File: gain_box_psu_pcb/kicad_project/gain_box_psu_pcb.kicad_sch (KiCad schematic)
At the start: 78 parts, among them J1 Conn_01x02, J2 Conn_01x04, J3 Conn_01x03, J4 Conn_01x02, J5 Conn_01x02, J6 AVR-UPDI-6, K1 J107F1CS2012VDC.80, K2 J104D2C12VDC.36S, Q1 AO3400A, Q2 AO3400A, Q3 AO3400A, T1 70042K, U1 LM7809, U2 LM7909, U3 78L05, U4 140817141310, U5 ATtiny412-SS

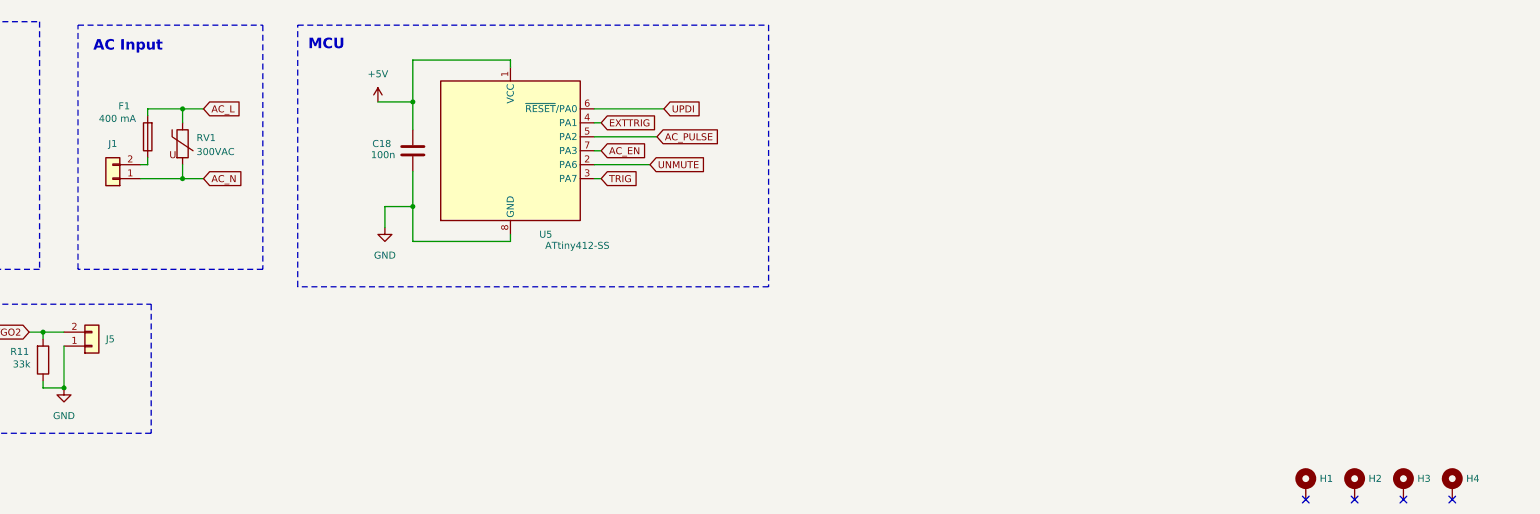
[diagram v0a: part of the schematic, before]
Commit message: Shorten PSU PCB
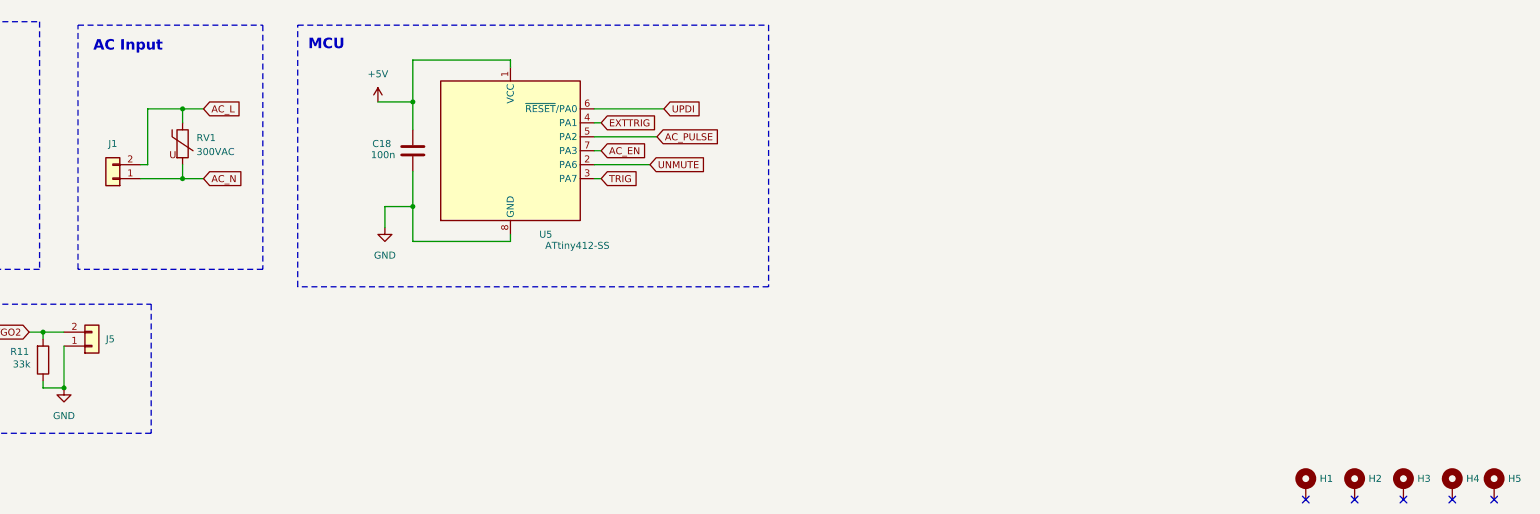
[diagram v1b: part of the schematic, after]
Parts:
- removed F1: 400 mA, Fuse:Fuseholder_Clip-5x20mm_Bel_FC-203-22_Lateral_P17.80x5.00mm_D1.17mm_Horizontal, symbol Device:Fuse
- added H5: MountingHole_Pad, MountingHole:MountingHole_3.2mm_M3_Pad_Via, symbol Mechanical:MountingHole_Pad
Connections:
- net AC_L: now also J1.2 (Pin_2)
- no-connect marks 6 -> 7
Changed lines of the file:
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@@
 	)
 	(no_connect
+		(at 397.51 246.38)
+	)
+	(no_connect
 		(at 363.22 246.38)
 	)
@@
 	(wire
 		(pts
-			(xy 152.4 175.26) (xy 152.4 176.53)
+			(xy 152.4 175.26) (xy 152.4 185.42)
 		)
 		(stroke
@@
 	(wire
 		(pts
-			(xy 152.4 184.15) (xy 152.4 185.42)
-		)
-		(stroke
-			(width 0)
-			(type default)
-		)
-	)
-	(wire
-		(pts
 			(xy 154.94 127) (xy 154.94 123.19)
 		)
@@
 	)
 	(symbol
+		(lib_id "Mechanical:MountingHole_Pad")
+		(at 397.51 243.84 0)
+		(unit 1)
+		(exclude_from_sim yes)
+		(in_bom no)
+		(on_board yes)
+		(dnp no)
+		(fields_autoplaced yes)
+		(property "Reference" "H5"
+			(at 400.05 242.5699 0)
+			(effects
+				(font
+					(size 1.27 1.27)
+				)
+				(justify left)
+			)
+		)
+		(property "Value" "MountingHole_Pad"
+			(at 400.05 243.8399 0)
+			(effects
+				(font
+					(size 1.27 1.27)
+				)
+				(justify left)
+				(hide yes)
+			)
+		)
+		(property "Footprint" "MountingHole:MountingHole_3.2mm_M3_Pad_Via"
+			(at 397.51 243.84 0)
+			(effects
+				(font
+					(size 1.27 1.27)
+				)
+				(hide yes)
+			)
+		)
+		(property "Datasheet" "~"
+			(at 397.51 243.84 0)
+			(effects
+				(font
+					(size 1.27 1.27)
+				)
+				(hide yes)
+			)
+		)
+		(property "Description" "Mounting Hole with connection"
+			(at 397.51 243.84 0)
+			(effects
+				(font
+					(size 1.27 1.27)
+				)
+				(hide yes)
+			)
+		)
+		(pin "1"
+		)
+		(instances
+			(project "gain_box_psu_pcb"
+				(path "/9bac93c0-f586-4b1c-8172-4868afdb9131"
+					(reference "H5")
+					(unit 1)
+				)
+			)
+		)
+	)
+	(symbol
 		(lib_id "Device:R")
 		(at 38.1 220.98 270)
@@
 					(unit 1)
 				)
-			)
-		)
-	)
-	(symbol
-		(lib_id "Device:Fuse")
-		(at 152.4 180.34 180)
-		(unit 1)
-		(exclude_from_sim no)
-		(in_bom yes)
-		(on_board yes)
-		(dnp no)
-		(property "Reference" "F1"
-			(at 147.066 174.752 0)
-			(effects
-				(font
-					(size 1.27 1.27)
-				)
-				(justify right)
-			)
-		)
-		(property "Value" "400 mA"
-			(at 143.51 177.038 0)
-			(effects
-				(font
-					(size 1.27 1.27)
-				)
-				(justify right)
-			)
-		)
-		(property "Footprint" "Fuse:Fuseholder_Clip-5x20mm_Bel_FC-203-22_Lateral_P17.80x5.00mm_D1.17mm_Horizontal"
-			(at 154.178 180.34 90)
-			(effects
-				(font
-					(size 1.27 1.27)
-				)
-				(hide yes)
-			)
-		)
-		(property "Datasheet" "~"
-			(at 152.4 180.34 0)
-			(effects
-				(font
-					(size 1.27 1.27)
-				)
-				(hide yes)
-			)
-		)
-		(property "Description" "Fuse"
-			(at 152.4 180.34 0)
-			(effects
-				(font
-					(size 1.27 1.27)
-				)
-				(hide yes)
-			)
-		)
-		(pin "2"
-		)
-		(pin "1"
-		)
-		(instances
-			(project ""
-				(path "/9bac93c0-f586-4b1c-8172-4868afdb9131"
-					(reference "F1")
-					(unit 1)
-				)

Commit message: Update PSU PCB
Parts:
- added H6: Screw_Terminal_01x01, project_lib:KEYSTONE_7760, symbol Connector:Screw_Terminal_01x01
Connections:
- net Earth: now reaches H2.1
- net Earth: now also H3.1, H6.1 (Pin_1)
- no-connect marks 7 -> 5
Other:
- moved on the sheet: H1, H2, H3
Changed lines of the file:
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@@
 	)
 	(junction
+		(at 358.14 236.22)
+		(diameter 0)
+		(color 0 0 0 0)
+	)
+	(junction
 		(at 69.85 69.85)
 		(diameter 0)
@@
 	)
 	(no_connect
-		(at 372.11 246.38)
-	)
-	(no_connect
 		(at 266.7 45.72)
 	)
@@
 	)
 	(no_connect
-		(at 363.22 246.38)
-	)
-	(no_connect
 		(at 381 246.38)
 	)
@@
 	(wire
 		(pts
+			(xy 349.25 236.22) (xy 358.14 236.22)
+		)
+		(stroke
+			(width 0)
+			(type default)
+		)
+	)
+	(wire
+		(pts
 			(xy 143.51 87.63) (xy 138.43 87.63)
 		)
@@
 	(wire
 		(pts
+			(xy 358.14 236.22) (xy 367.03 236.22)
+		)
+		(stroke
+			(width 0)
+			(type default)
+		)
+	)
+	(wire
+		(pts
 			(xy 73.66 137.16) (xy 73.66 139.7)
 		)
@@
 	(wire
 		(pts
+			(xy 358.14 236.22) (xy 358.14 241.3)
+		)
+		(stroke
+			(width 0)
+			(type default)
+		)
+	)
+	(wire
+		(pts
 			(xy 367.03 77.47) (xy 369.57 77.47)
 		)
@@
 	(wire
 		(pts
+			(xy 367.03 236.22) (xy 367.03 234.95)
+		)
+		(stroke
+			(width 0)
+			(type default)
+		)
+	)
+	(wire
+		(pts
 			(xy 378.46 113.03) (xy 378.46 115.57)
 		)
@@
 	(wire
 		(pts
+			(xy 349.25 234.95) (xy 349.25 236.22)
+		)
+		(stroke
+			(width 0)
+			(type default)
+		)
+	)
+	(wire
+		(pts
 			(xy 186.69 54.61) (xy 186.69 59.69)
 		)
@@
 		)
 	)
+	(wire
+		(pts
+			(xy 358.14 236.22) (xy 358.14 234.95)
+		)
+		(stroke
+			(width 0)
+			(type default)
+		)
+	)
 	(rectangle
 		(start 17.78 104.14)
@@
 	)
 	(symbol
+		(lib_id "power:Earth")
+		(at 358.14 241.3 0)
+		(unit 1)
+		(exclude_from_sim no)
+		(in_bom yes)
+		(on_board yes)
+		(dnp no)
+		(fields_autoplaced yes)
+		(property "Reference" "#PWR01"
+			(at 358.14 247.65 0)
+			(effects
+				(font
+					(size 1.27 1.27)
+				)
+				(hide yes)
+			)
+		)
+		(property "Value" "Earth"
+			(at 358.14 246.38 0)
+			(effects
+				(font
+					(size 1.27 1.27)
+				)
+			)
+		)
+		(property "Footprint" ""
+			(at 358.14 241.3 0)
+			(effects
+				(font
+					(size 1.27 1.27)
+				)
+				(hide yes)
+			)
+		)
+		(property "Datasheet" "~"
+			(at 358.14 241.3 0)
+			(effects
+				(font
+					(size 1.27 1.27)
+				)
+				(hide yes)
+			)
+		)
+		(property "Description" "Power symbol creates a global label with name \"Earth\""
+			(at 358.14 241.3 0)
+			(effects
+				(font
+					(size 1.27 1.27)
+				)
+				(hide yes)
+			)
+		)
+		(pin "1"
+		)
+		(instances
+			(project ""
+				(path "/9bac93c0-f586-4b1c-8172-4868afdb9131"
+					(reference "#PWR01")
+					(unit 1)
+				)
+			)
+		)
+	)
+	(symbol
 		(lib_id "power:+15V")
 		(at 194.31 39.37 0)
@@
 	(symbol
 		(lib_id "Mechanical:MountingHole_Pad")
-		(at 372.11 243.84 0)
+		(at 358.14 232.41 0)
 		(unit 1)
 		(exclude_from_sim yes)
@@
 		(fields_autoplaced yes)
 		(property "Reference" "H2"
-			(at 374.65 242.5699 0)
+			(at 360.68 231.1399 0)
 			(effects
 				(font
@@
 		)
 		(property "Value" "MountingHole_Pad"
-			(at 374.65 243.8399 0)
+			(at 360.68 232.4099 0)
 			(effects
 				(font
@@
 		)
 		(property "Footprint" "MountingHole:MountingHole_3.2mm_M3_Pad_Via"
-			(at 372.11 243.84 0)
+			(at 358.14 232.41 0)
 			(effects
 				(font
@@
 		)
 		(property "Datasheet" "~"
-			(at 372.11 243.84 0)
+			(at 358.14 232.41 0)
 			(effects
 				(font
@@
 		)
 		(property "Description" "Mounting Hole with connection"
-			(at 372.11 243.84 0)
+			(at 358.14 232.41 0)
 			(effects
 				(font
@@
 	(symbol
 		(lib_id "Mechanical:MountingHole_Pad")
-		(at 381 243.84 0)
+		(at 367.03 232.41 0)
 		(unit 1)
 		(exclude_from_sim yes)
@@
 		(fields_autoplaced yes)
 		(property "Reference" "H3"
-			(at 383.54 242.5699 0)
+			(at 369.57 231.1399 0)
 			(effects
 				(font
@@
 		)
 		(property "Value" "MountingHole_Pad"
-			(at 383.54 243.8399 0)
+			(at 369.57 232.4099 0)
 			(effects
 				(font
@@
 		)
 		(property "Footprint" "MountingHole:MountingHole_3.2mm_M3_Pad_Via"
-			(at 381 243.84 0)
+			(at 367.03 232.41 0)
 			(effects
 				(font
@@
 		)
 		(property "Datasheet" "~"
-			(at 381 243.84 0)
+			(at 367.03 232.41 0)
 			(effects
 				(font
@@
 		)
 		(property "Description" "Mounting Hole with connection"
-			(at 381 243.84 0)
+			(at 367.03 232.41 0)
 			(effects
 				(font
@@
 	(symbol
 		(lib_id "Mechanical:MountingHole_Pad")
-		(at 363.22 243.84 0)
+		(at 381 243.84 0)
 		(unit 1)
 		(exclude_from_sim yes)
@@
 		(fields_autoplaced yes)
 		(property "Reference" "H1"
-			(at 365.76 242.5699 0)
+			(at 383.54 242.5699 0)
 			(effects
 				(font
@@
 		)
 		(property "Value" "MountingHole_Pad"
-			(at 365.76 243.8399 0)
+			(at 383.54 243.8399 0)
 			(effects
 				(font
@@
 		)
 		(property "Footprint" "MountingHole:MountingHole_3.2mm_M3_Pad_Via"
-			(at 363.22 243.84 0)
+			(at 381 243.84 0)
 			(effects
 				(font
@@
 		)
 		(property "Datasheet" "~"
-			(at 363.22 243.84 0)
+			(at 381 243.84 0)
 			(effects
 				(font
@@
 		)
 		(property "Description" "Mounting Hole with connection"
-			(at 363.22 243.84 0)
+			(at 381 243.84 0)
 			(effects
 				(font
@@
 					(unit 1)
 				)
+			)
+		)
+	)
+	(symbol
+		(lib_id "Connector:Screw_Terminal_01x01")
+		(at 349.25 229.87 90)
+		(unit 1)
+		(exclude_from_sim no)
+		(in_bom yes)
+		(on_board yes)
+		(dnp no)
+		(fields_autoplaced yes)
+		(property "Reference" "H6"
+			(at 351.79 229.8699 90)
+			(effects
+				(font
+					(size 1.27 1.27)
+				)
+				(justify right)
+			)
+		)
+		(property "Value" "Screw_Terminal_01x01"
+			(at 350.5199 227.33 0)
+			(effects
+				(font
+					(size 1.27 1.27)
+				)
+				(justify left)
+				(hide yes)
+			)
+		)
+		(property "Footprint" "project_lib:KEYSTONE_7760"
+			(at 349.25 229.87 0)
+			(effects
+				(font
+					(size 1.27 1.27)
+				)
+				(hide yes)
+			)
+		)
+		(property "Datasheet" "~"
+			(at 349.25 229.87 0)
+			(effects
+				(font
+					(size 1.27 1.27)
+				)
+				(hide yes)
+			)
+		)
+		(property "Description" "Generic screw terminal, single row, 01x01, script generated (kicad-library-utils/schlib/autogen/connector/)"
+			(at 349.25 229.87 0)
+			(effects
+				(font
+					(size 1.27 1.27)
+				)
+				(hide yes)
+			)
+		)
+		(pin "1"
+		)
+		(instances
+			(project ""
+				(path "/9bac93c0-f586-4b1c-8172-4868afdb9131"
+					(reference "H6")
+					(unit 1)
+				)

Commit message: New main PSU caps
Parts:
- C1, C2, C3, C4: footprint Capacitor_THT:CP_Radial_D16.0mm_P7.50mm -> Capacitor_THT:CP_Radial_D18.0mm_P7.50mm
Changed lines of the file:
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@@
 			)
 		)
-		(property "Footprint" "Capacitor_THT:CP_Radial_D16.0mm_P7.50mm"
+		(property "Footprint" "Capacitor_THT:CP_Radial_D18.0mm_P7.50mm"
 			(at 103.8352 72.39 0)
 			(effects
@@
 			)
 		)
-		(property "Footprint" "Capacitor_THT:CP_Radial_D16.0mm_P7.50mm"
+		(property "Footprint" "Capacitor_THT:CP_Radial_D18.0mm_P7.50mm"
 			(at 119.0752 72.39 0)
 			(effects
@@
 			)
 		)
-		(property "Footprint" "Capacitor_THT:CP_Radial_D16.0mm_P7.50mm"
+		(property "Footprint" "Capacitor_THT:CP_Radial_D18.0mm_P7.50mm"
 			(at 103.8352 54.61 0)
 			(effects
@@
 			)
 		)
-		(property "Footprint" "Capacitor_THT:CP_Radial_D16.0mm_P7.50mm"
+		(property "Footprint" "Capacitor_THT:CP_Radial_D18.0mm_P7.50mm"
 			(at 119.0752 54.61 0)
 			(effects

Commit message: Sent to production
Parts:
- T1: value 70042K -> 70023K; footprint project_lib:XFMR_70042K -> project_lib:TRANS_Talema_70023K; symbol gain_box:70042K -> project_lib:TRANS_Talema_700xxK
- U1: value LM7809 -> LM7812; symbol Regulator_Linear:LM7809_TO220 -> Regulator_Linear:LM7812_TO220
- U2: value LM7909 -> LM7912; symbol Regulator_Linear:LM7909_TO220 -> Regulator_Linear:LM7912_TO220
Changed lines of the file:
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@@
 	)
 	(symbol
-		(lib_id "Regulator_Linear:LM7909_TO220")
+		(lib_id "Regulator_Linear:LM7912_TO220")
 		(at 147.32 76.2 0)
 		(unit 1)
@@
 			)
 		)
-		(property "Value" "LM7909"
+		(property "Value" "LM7912"
 			(at 147.32 82.55 0)
 			(effects
@@
 			)
 		)
-		(property "Datasheet" "https://www.onsemi.com/pub/Collateral/MC7900-D.PDF"
+		(property "Datasheet" "hhttps://www.onsemi.com/pub/Collateral/MC7900-D.PDF"
 			(at 147.32 76.2 0)
 			(effects
@@
 			)
 		)
-		(property "Description" "Negative 1A 35V Linear Regulator, Fixed Output 9V, TO-220"
+		(property "Description" "Negative 1A 35V Linear Regulator, Fixed Output 12V, TO-220"
 			(at 147.32 76.2 0)
 			(effects
@@
 	)
 	(symbol
-		(lib_id "Regulator_Linear:LM7809_TO220")
+		(lib_id "Regulator_Linear:LM7812_TO220")
 		(at 147.32 41.91 0)
 		(unit 1)
@@
 			)
 		)
-		(property "Value" "LM7809"
+		(property "Value" "LM7812"
 			(at 147.32 38.1 0)
 			(effects
@@
 			)
 		)
-		(property "Description" "Positive 1A 35V Linear Regulator, Fixed Output 9V, TO-220"
+		(property "Description" "Positive 1A 35V Linear Regulator, Fixed Output 12V, TO-220"
 			(at 147.32 41.91 0)
 			(effects
@@
 	)
 	(symbol
-		(lib_id "gain_box:70042K")
+		(lib_id "project_lib:TRANS_Talema_700xxK")
 		(at 58.42 59.69 0)
 		(unit 1)
@@
 		(fields_autoplaced yes)
 		(property "Reference" "T1"
-			(at 58.8214 41.91 0)
+			(at 58.5674 41.91 0)
 			(effects
 				(font
@@
 			)
 		)
-		(property "Value" "70042K"
-			(at 58.8214 44.45 0)
+		(property "Value" "70023K"
+			(at 58.5674 44.45 0)
 			(effects
 				(font
@@
 			)
 		)
-		(property "Footprint" "project_lib:XFMR_70042K"
+		(property "Footprint" "project_lib:TRANS_Talema_70023K"
 			(at 58.42 59.69 0)
 			(effects
